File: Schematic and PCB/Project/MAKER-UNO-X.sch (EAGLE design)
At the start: 101 parts, among them CN1 USB-5PIN_(MICRO-B-RA), Q1 60V 600mA, Q10 50V 220mA, Q11 50V 220mA, Q12 50V 220mA, Q13 50V 220mA, Q14 50V 220mA, Q2 50V 220mA, Q3 50V 220mA, Q4 50V 220mA, Q5 50V 220mA, Q6 50V 220mA, Q7 50V 220mA, Q8 50V 220mA, Q9 50V 220mA, U2 CH340G_CH340C_(SOIC-16N), U3 555_(SOIC-08N), U4 3.3V 500mA, Y1 16MHz

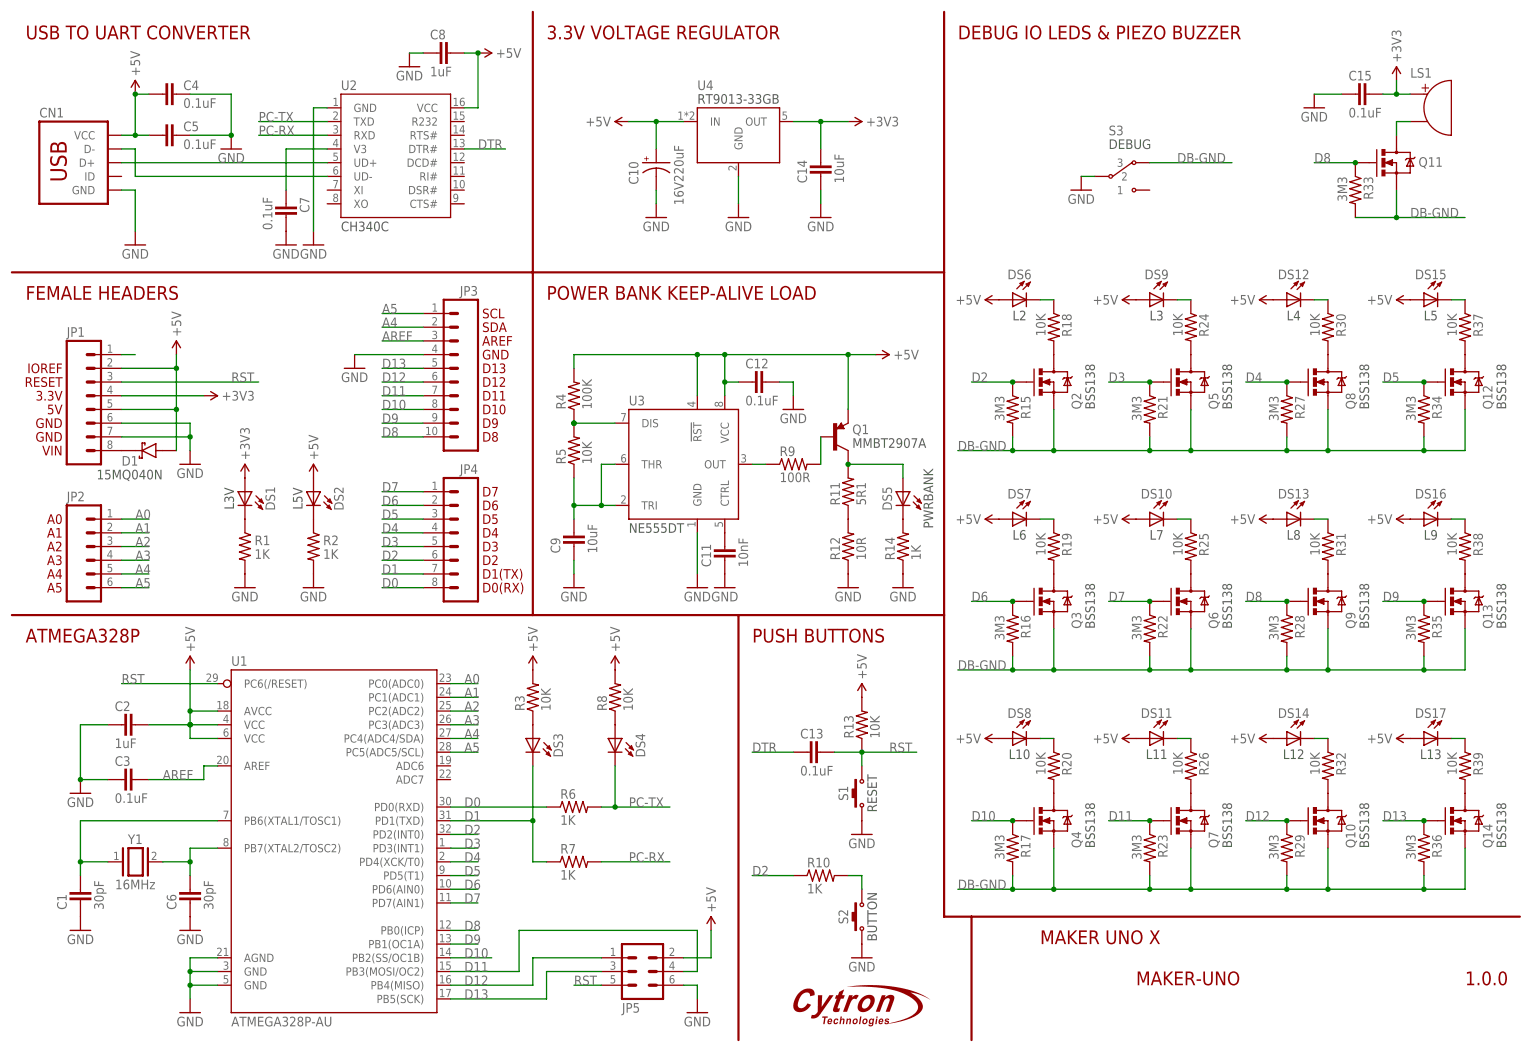
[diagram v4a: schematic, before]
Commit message: Fixed the problem of the debug switch and strengthen the mouse bite.
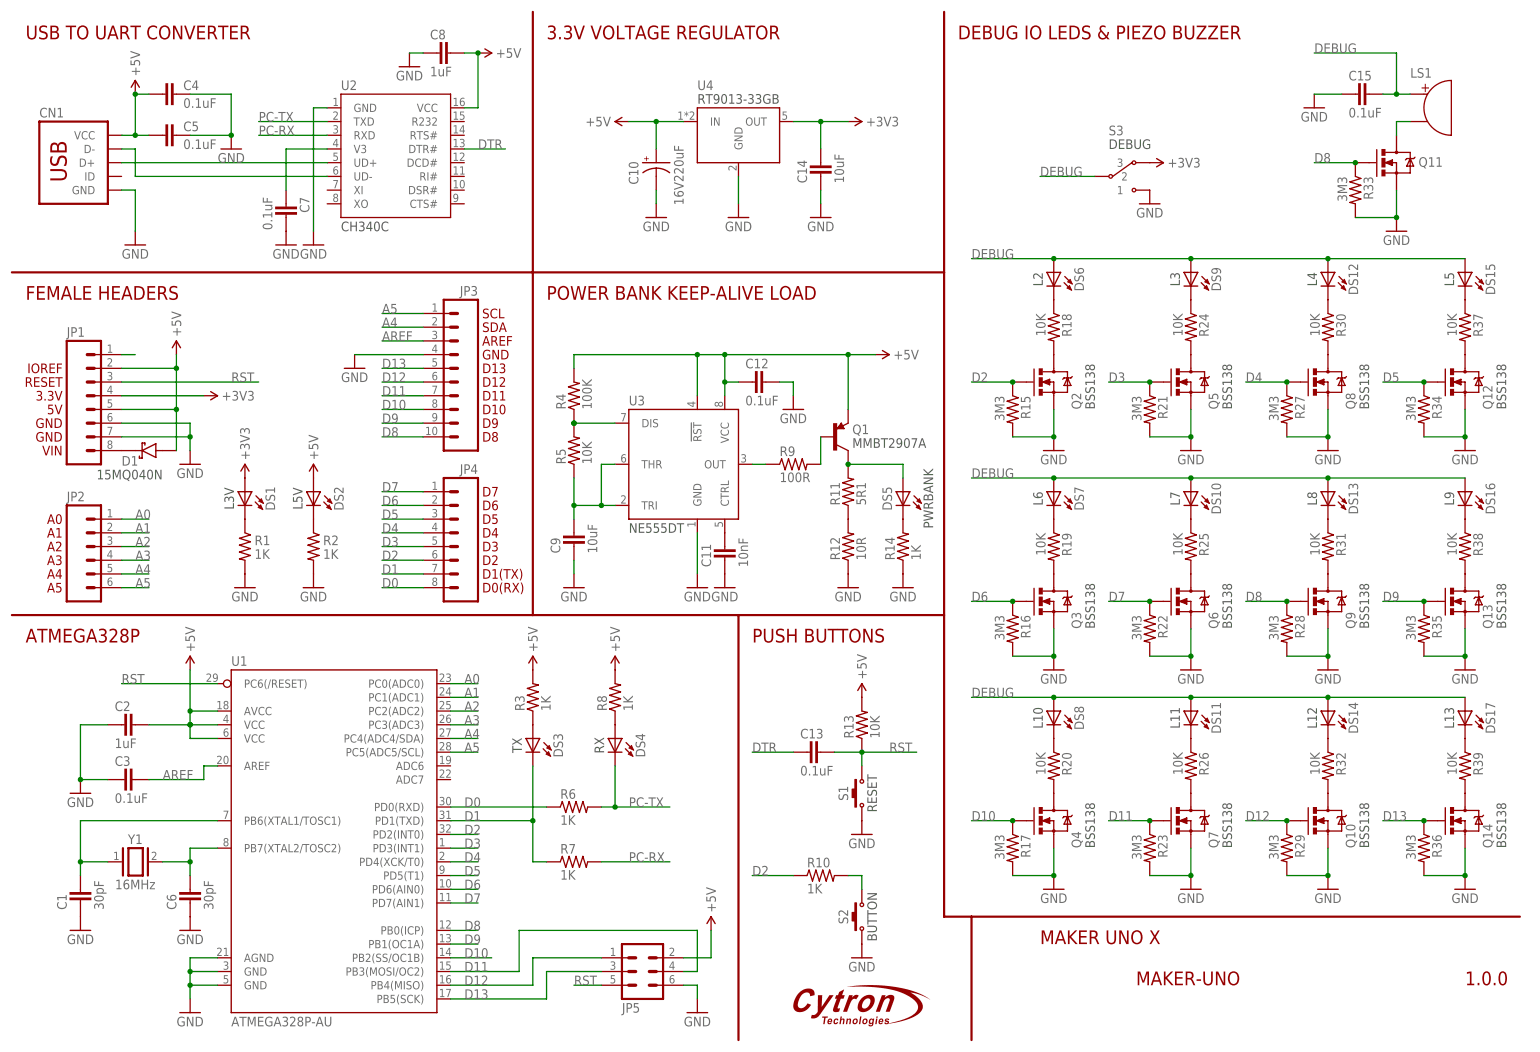
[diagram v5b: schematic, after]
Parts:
- DS3: LABEL (none) -> TX
- DS4: LABEL (none) -> RX
- R3, R8: value 10K -> 1K; device Others:RESISTOR_10K_(1608) -> Others:RESISTOR_1K_(1608)
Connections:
- removed net DB-GND: Q10.S, Q11.S, Q12.S, Q13.S, Q14.S, Q2.S, Q3.S, Q4.S, Q5.S, Q6.S, Q7.S, Q8.S, Q9.S, R15.2, R16.2, R17.2, R21.2, R22.2, R23.2, R27.2, R28.2, R29.2, R33.2, R34.2, R35.2, R36.2, S3.3
- new net DEBUG: C15.1, DS10.A, DS11.A, DS12.A, DS13.A, DS14.A, DS15.A, DS16.A, DS17.A, DS6.A, DS7.A, DS8.A, DS9.A, LS1.+, S3.2
- net +3V3: now also S3.3; no longer C15.1, LS1.+
- net +5V: no longer DS10.A, DS11.A, DS12.A, DS13.A, DS14.A, DS15.A, DS16.A, DS17.A, DS6.A, DS7.A, DS8.A, DS9.A
- net GND: now also Q10.S, Q11.S, Q12.S, Q13.S, Q14.S, Q2.S, Q3.S, Q4.S, Q5.S, Q6.S, Q7.S, Q8.S, Q9.S, R15.2, R16.2, R17.2, R21.2, R22.2, R23.2, R27.2, R28.2, R29.2, R33.2, R34.2, R35.2, R36.2, S3.1; no longer S3.2
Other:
- moved on the sheet: DS10, DS11, DS12, DS13, DS14, DS15, DS16, DS17, DS6, DS7, DS8, DS9

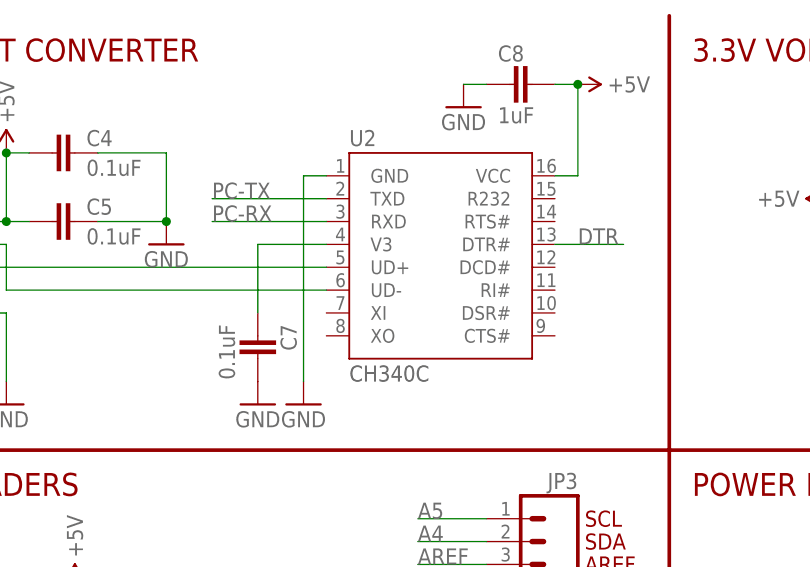
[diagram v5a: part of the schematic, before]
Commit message: Replaced CH340C with CH9340C.
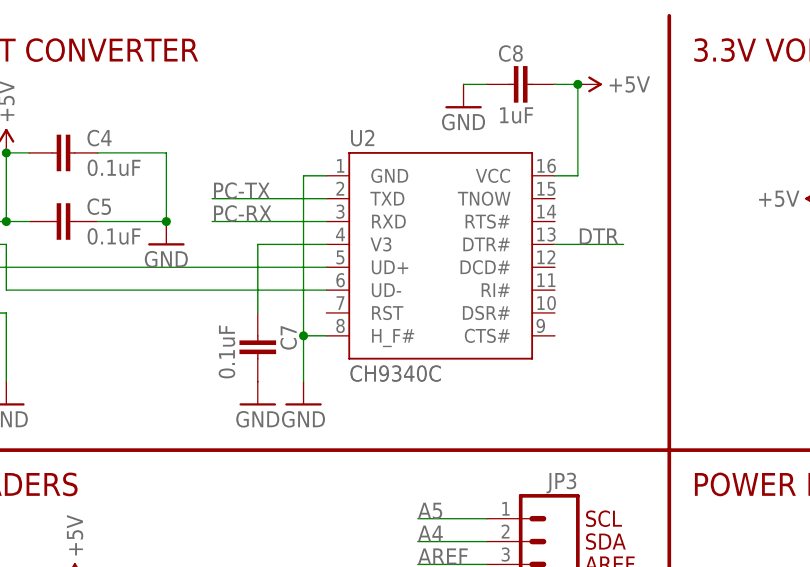
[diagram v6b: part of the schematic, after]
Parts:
- U2: value CH340G_CH340C_(SOIC-16N) -> CH9340C; device IC & Transistor:CH340G_CH340C_(SOIC-16N) -> IC & Transistor:CH9340C
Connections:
- net GND: now also U2.H_F#
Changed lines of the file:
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@@
 <part name="JP4" library="Header and Connector" deviceset="HEADER-1X08" device="_(SMD-FEMALE-TYPE1)" value="8 Ways"/>
 <part name="JP3" library="Header and Connector" deviceset="HEADER-1X10" device="_(SMD-FEMALE-TYPE1)" value="10 Ways"/>
-<part name="U2" library="IC &amp; Transistor" deviceset="CH340G" device="_(SOIC-16N)" technology="_CH340C" value=""/>
+<part name="U2" library="IC &amp; Transistor" deviceset="CH9340C" device="" value=""/>
 <part name="DS17" library="Others" deviceset="LED" device="_(1608)" technology="_BLUE" value="Blue">
 <attribute name="LABEL" value="L13"/>
@@
 <pinref part="U2" gate="G$1" pin="GND"/>
 <pinref part="GND18" gate="1" pin="GND"/>
-<wire x1="55.88" y1="149.86" x2="55.88" y2="172.72" width="0.1524" layer="91"/>
+<wire x1="55.88" y1="149.86" x2="55.88" y2="154.94" width="0.1524" layer="91"/>
+<wire x1="55.88" y1="154.94" x2="55.88" y2="172.72" width="0.1524" layer="91"/>
 <wire x1="55.88" y1="172.72" x2="58.42" y2="172.72" width="0.1524" layer="91"/>
+<pinref part="U2" gate="G$1" pin="H_F#"/>
+<wire x1="58.42" y1="154.94" x2="55.88" y2="154.94" width="0.1524" layer="91"/>
+<junction x="55.88" y="154.94"/>
 </segment>
 <segment>
